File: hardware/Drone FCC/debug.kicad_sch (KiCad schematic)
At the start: 1 part, among them J22 Conn_02x05_Odd_Even

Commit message: finished IMU basic schematic
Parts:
- added J?: Conn_02x02_Counter_Clockwise, symbol Connector_Generic:Conn_02x02_Counter_Clockwise
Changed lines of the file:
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@@
     (pin "9")
   )
+  (symbol (lib_id "Connector_Generic:Conn_02x02_Counter_Clockwise") (at 104.775 75.565 0) (unit 1)
+    (in_bom yes) (on_board yes) (fields_autoplaced)
+    (property "Reference" "J?" (id 0) (at 106.045 68.58 0))
+    (property "Value" "Conn_02x02_Counter_Clockwise" (id 1) (at 106.045 71.12 0))
+    (property "Footprint" "" (id 2) (at 104.775 75.565 0)
+      (effects (font (size 1.27 1.27)) hide)
+    )
+    (property "Datasheet" "~" (id 3) (at 104.775 75.565 0)
+      (effects (font (size 1.27 1.27)) hide)
+    )
+    (pin "1")
+    (pin "2")
+    (pin "3")
+    (pin "4")
+  )
 )

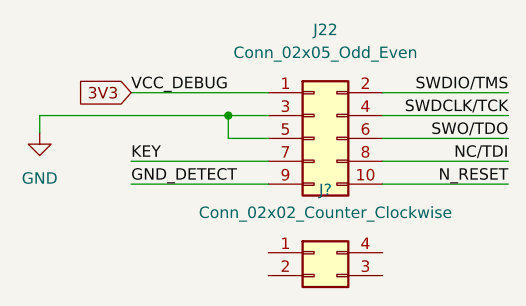
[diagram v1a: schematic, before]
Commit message: finish barometer schematic
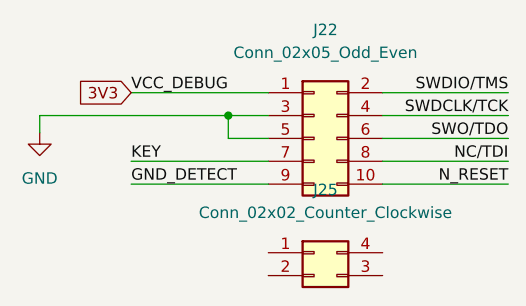
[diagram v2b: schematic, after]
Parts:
- gave numbers to parts that had none: 1
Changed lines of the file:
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@@
   (symbol (lib_id "Connector_Generic:Conn_02x02_Counter_Clockwise") (at 104.775 75.565 0) (unit 1)
     (in_bom yes) (on_board yes) (fields_autoplaced)
-    (property "Reference" "J?" (id 0) (at 106.045 68.58 0))
+    (property "Reference" "J25" (id 0) (at 106.045 68.58 0))
     (property "Value" "Conn_02x02_Counter_Clockwise" (id 1) (at 106.045 71.12 0))
     (property "Footprint" "" (id 2) (at 104.775 75.565 0)

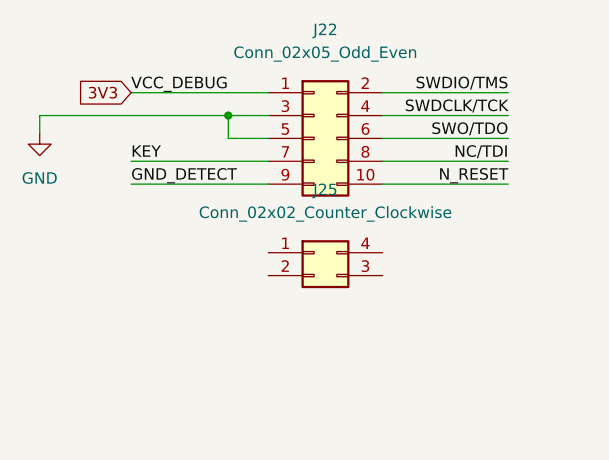
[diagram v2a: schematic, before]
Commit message: finish SWD functional schematic
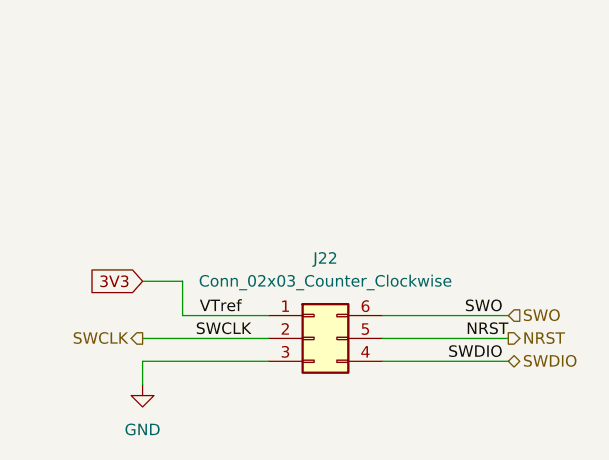
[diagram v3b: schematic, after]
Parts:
- removed J22: Conn_02x05_Odd_Even, FTSH-105-01-F-DV-K-TR:SAMTEC_FTSH-105-01-F-DV-P-TR, symbol Connector_Generic:Conn_02x05_Odd_Even
- removed J25: Conn_02x02_Counter_Clockwise, symbol Connector_Generic:Conn_02x02_Counter_Clockwise
- added J22: Conn_02x03_Counter_Clockwise, Connector_PinHeader_2.54mm:PinHeader_2x03_P2.54mm_Vertical, symbol Connector_Generic:Conn_02x03_Counter_Clockwise
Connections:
- net 3V3: now also J22.1 (Pin_1)
- net GND: now also J22.3 (Pin_3)
- new net NRST: J22.5 (Pin_5)
- new net SWCLK: J22.2 (Pin_2)
- new net SWDIO: J22.4 (Pin_4)
- new net SWO: J22.6 (Pin_6)
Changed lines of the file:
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@@
 (kicad_sch (version 20211123) (generator eeschema)
   (paper "A4")
-  (junction (at 95.25 60.325) (diameter 0) (color 0 0 0 0)
-  )
-  (wire (pts (xy 84.455 57.785) (xy 99.695 57.785))
+  (wire (pts (xy 90.17 78.74) (xy 90.17 82.55))
     (stroke (width 0) (type default) (color 0 0 0 0))
   )
-  (wire (pts (xy 95.25 62.865) (xy 95.25 60.325))
+  (wire (pts (xy 112.395 82.55) (xy 126.365 82.55))
     (stroke (width 0) (type default) (color 0 0 0 0))
   )
-  (wire (pts (xy 74.295 60.325) (xy 74.295 62.23))
+  (wire (pts (xy 85.725 87.63) (xy 99.695 87.63))
     (stroke (width 0) (type default) (color 0 0 0 0))
   )
-  (wire (pts (xy 112.395 62.865) (xy 126.365 62.865))
+  (wire (pts (xy 85.725 87.63) (xy 85.725 90.17))
     (stroke (width 0) (type default) (color 0 0 0 0))
   )
-  (wire (pts (xy 95.25 60.325) (xy 99.695 60.325))
+  (wire (pts (xy 112.395 85.09) (xy 126.365 85.09))
     (stroke (width 0) (type default) (color 0 0 0 0))
   )
-  (wire (pts (xy 84.455 67.945) (xy 99.695 67.945))
+  (wire (pts (xy 85.725 85.09) (xy 99.695 85.09))
     (stroke (width 0) (type default) (color 0 0 0 0))
   )
-  (wire (pts (xy 112.395 57.785) (xy 126.365 57.785))
+  (wire (pts (xy 112.395 87.63) (xy 126.365 87.63))
     (stroke (width 0) (type default) (color 0 0 0 0))
   )
-  (wire (pts (xy 84.455 65.405) (xy 99.695 65.405))
+  (wire (pts (xy 85.725 78.74) (xy 90.17 78.74))
     (stroke (width 0) (type default) (color 0 0 0 0))
   )
-  (wire (pts (xy 112.395 67.945) (xy 126.365 67.945))
+  (wire (pts (xy 90.17 82.55) (xy 99.695 82.55))
     (stroke (width 0) (type default) (color 0 0 0 0))
   )
-  (wire (pts (xy 99.695 62.865) (xy 95.25 62.865))
-    (stroke (width 0) (type default) (color 0 0 0 0))
+  (label "SWDIO" (at 125.73 87.63 180)
+    (effects (font (size 1.27 1.27)) (justify right bottom))
   )
-  (wire (pts (xy 74.295 60.325) (xy 95.25 60.325))
-    (stroke (width 0) (type default) (color 0 0 0 0))
-  )
-  (wire (pts (xy 112.395 60.325) (xy 126.365 60.325))
-    (stroke (width 0) (type default) (color 0 0 0 0))
-  )
-  (wire (pts (xy 112.395 65.405) (xy 126.365 65.405))
-    (stroke (width 0) (type default) (color 0 0 0 0))
-  )
-  (label "VCC_DEBUG" (at 84.455 57.785 0)
+  (label "VTref" (at 92.075 82.55 0)
     (effects (font (size 1.27 1.27)) (justify left bottom))
   )
-  (label "GND_DETECT" (at 84.455 67.945 0)
-    (effects (font (size 1.27 1.27)) (justify left bottom))
-  )
-  (label "N_RESET" (at 126.365 67.945 180)
+  (label "SWCLK" (at 97.79 85.09 180)
     (effects (font (size 1.27 1.27)) (justify right bottom))
   )
-  (label "SWO{slash}TDO" (at 126.365 62.865 180)
+  (label "NRST" (at 126.365 85.09 180)
     (effects (font (size 1.27 1.27)) (justify right bottom))
   )
-  (label "SWDCLK{slash}TCK" (at 126.365 60.325 180)
+  (label "SWO" (at 125.73 82.55 180)
     (effects (font (size 1.27 1.27)) (justify right bottom))
   )
-  (label "NC{slash}TDI" (at 126.365 65.405 180)
-    (effects (font (size 1.27 1.27)) (justify right bottom))
-  )
-  (label "SWDIO{slash}TMS" (at 126.365 57.785 180)
-    (effects (font (size 1.27 1.27)) (justify right bottom))
-  )
-  (label "KEY" (at 84.455 65.405 0)
-    (effects (font (size 1.27 1.27)) (justify left bottom))
-  )
-  (global_label "3V3" (shape input) (at 84.455 57.785 180) (fields_autoplaced)
+  (global_label "3V3" (shape input) (at 85.725 78.74 180) (fields_autoplaced)
     (effects (font (size 1.27 1.27)) (justify right))
-    (property "Intersheet References" "${INTERSHEET_REFS}" (id 0) (at 78.5343 57.7056 0)
+    (property "Intersheet References" "${INTERSHEET_REFS}" (id 0) (at 79.8043 78.6606 0)
       (effects (font (size 1.27 1.27)) (justify right) hide)
     )
   )
-  (symbol (lib_id "power:GND") (at 74.295 62.23 0) (unit 1)
+  (hierarchical_label "SWCLK" (shape output) (at 85.725 85.09 180)
+    (effects (font (size 1.27 1.27)) (justify right))
+  )
+  (hierarchical_label "NRST" (shape output) (at 126.365 85.09 0)
+    (effects (font (size 1.27 1.27)) (justify left))
+  )
+  (hierarchical_label "SWO" (shape input) (at 126.365 82.55 0)
+    (effects (font (size 1.27 1.27)) (justify left))
+  )
+  (hierarchical_label "SWDIO" (shape bidirectional) (at 126.365 87.63 0)
+    (effects (font (size 1.27 1.27)) (justify left))
+  )
+  (symbol (lib_id "power:GND") (at 85.725 90.17 0) (unit 1)
     (in_bom yes) (on_board yes) (fields_autoplaced)
-    (property "Reference" "#PWR0118" (id 0) (at 74.295 68.58 0)
+    (property "Reference" "#PWR0118" (id 0) (at 85.725 96.52 0)
       (effects (font (size 1.27 1.27)) hide)
     )
-    (property "Value" "GND" (id 1) (at 74.295 67.31 0))
-    (property "Footprint" "" (id 2) (at 74.295 62.23 0)
+    (property "Value" "GND" (id 1) (at 85.725 95.25 0))
+    (property "Footprint" "" (id 2) (at 85.725 90.17 0)
       (effects (font (size 1.27 1.27)) hide)
     )
-    (property "Datasheet" "" (id 3) (at 74.295 62.23 0)
+    (property "Datasheet" "" (id 3) (at 85.725 90.17 0)
       (effects (font (size 1.27 1.27)) hide)
     )
     (pin "1")
   )
-  (symbol (lib_id "Connector_Generic:Conn_02x05_Odd_Even") (at 104.775 62.865 0) (unit 1)
+  (symbol (lib_id "Connector_Generic:Conn_02x03_Counter_Clockwise") (at 104.775 85.09 0) (unit 1)
     (in_bom yes) (on_board yes) (fields_autoplaced)
-    (property "Reference" "J22" (id 0) (at 106.045 50.8 0))
-    (property "Value" "Conn_02x05_Odd_Even" (id 1) (at 106.045 53.34 0))
-    (property "Footprint" "FTSH-105-01-F-DV-K-TR:SAMTEC_FTSH-105-01-F-DV-P-TR" (id 2) (at 104.775 62.865 0)
+    (property "Reference" "J22" (id 0) (at 106.045 76.2 0))
+    (property "Value" "Conn_02x03_Counter_Clockwise" (id 1) (at 106.045 78.74 0))
+    (property "Footprint" "Connector_PinHeader_2.54mm:PinHeader_2x03_P2.54mm_Vertical" (id 2) (at 104.775 85.09 0)
       (effects (font (size 1.27 1.27)) hide)
     )
-    (property "Datasheet" "~" (id 3) (at 104.775 62.865 0)
-      (effects (font (size 1.27 1.27)) hide)
-    )
-    (pin "1")
-    (pin "10")
-    (pin "2")
-    (pin "3")
-    (pin "4")
-    (pin "5")
-    (pin "6")
-    (pin "7")
-    (pin "8")
-    (pin "9")
-  )
-  (symbol (lib_id "Connector_Generic:Conn_02x02_Counter_Clockwise") (at 104.775 75.565 0) (unit 1)
-    (in_bom yes) (on_board yes) (fields_autoplaced)
-    (property "Reference" "J25" (id 0) (at 106.045 68.58 0))
-    (property "Value" "Conn_02x02_Counter_Clockwise" (id 1) (at 106.045 71.12 0))
-    (property "Footprint" "" (id 2) (at 104.775 75.565 0)
-      (effects (font (size 1.27 1.27)) hide)
-    )
-    (property "Datasheet" "~" (id 3) (at 104.775 75.565 0)
+    (property "Datasheet" "~" (id 3) (at 104.775 85.09 0)
       (effects (font (size 1.27 1.27)) hide)
     )
@@
     (pin "3")
     (pin "4")
+    (pin "5")
+    (pin "6")
   )
 )

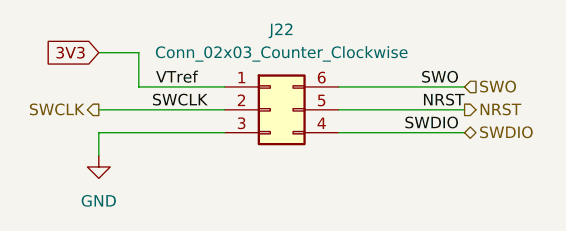
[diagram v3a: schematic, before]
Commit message: re enumeration of components
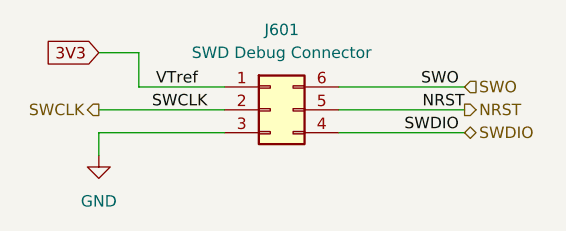
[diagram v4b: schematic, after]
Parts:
- J601: renamed from J22; value Conn_02x03_Counter_Clockwise -> SWD Debug Connector
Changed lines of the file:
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@@
   (symbol (lib_id "Connector_Generic:Conn_02x03_Counter_Clockwise") (at 104.775 85.09 0) (unit 1)
     (in_bom yes) (on_board yes) (fields_autoplaced)
-    (property "Reference" "J22" (id 0) (at 106.045 76.2 0))
-    (property "Value" "Conn_02x03_Counter_Clockwise" (id 1) (at 106.045 78.74 0))
+    (property "Reference" "J601" (id 0) (at 106.045 76.2 0))
+    (property "Value" "SWD Debug Connector" (id 1) (at 106.045 78.74 0))
     (property "Footprint" "Connector_PinHeader_2.54mm:PinHeader_2x03_P2.54mm_Vertical" (id 2) (at 104.775 85.09 0)
       (effects (font (size 1.27 1.27)) hide)

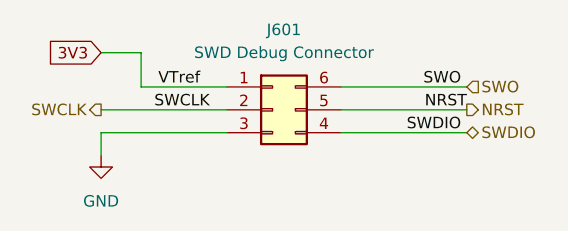
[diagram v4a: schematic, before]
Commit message: included all components on PCB
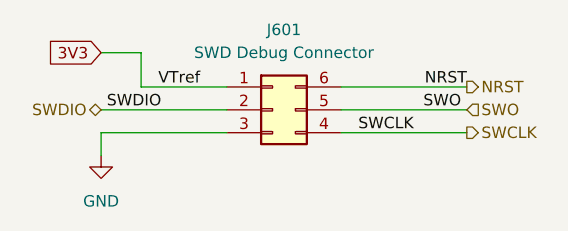
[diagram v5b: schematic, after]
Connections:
- net NRST: now also J601.6 (Pin_6); no longer J601.5 (Pin_5)
- net SWCLK: now also J601.4 (Pin_4); no longer J601.2 (Pin_2)
- net SWDIO: now also J601.2 (Pin_2); no longer J601.4 (Pin_4)
- net SWO: now also J601.5 (Pin_5); no longer J601.6 (Pin_6)
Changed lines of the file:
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@@
     (stroke (width 0) (type default) (color 0 0 0 0))
   )
-  (wire (pts (xy 112.395 82.55) (xy 126.365 82.55))
+  (wire (pts (xy 112.395 85.09) (xy 126.365 85.09))
     (stroke (width 0) (type default) (color 0 0 0 0))
   )
@@
     (stroke (width 0) (type default) (color 0 0 0 0))
   )
-  (wire (pts (xy 112.395 85.09) (xy 126.365 85.09))
+  (wire (pts (xy 112.395 82.55) (xy 126.365 82.55))
     (stroke (width 0) (type default) (color 0 0 0 0))
   )
-  (wire (pts (xy 85.725 85.09) (xy 99.695 85.09))
+  (wire (pts (xy 126.365 87.63) (xy 112.395 87.63))
     (stroke (width 0) (type default) (color 0 0 0 0))
   )
-  (wire (pts (xy 112.395 87.63) (xy 126.365 87.63))
+  (wire (pts (xy 99.695 85.09) (xy 85.725 85.09))
     (stroke (width 0) (type default) (color 0 0 0 0))
   )
@@
     (stroke (width 0) (type default) (color 0 0 0 0))
   )
-  (label "SWDIO" (at 125.73 87.63 180)
-    (effects (font (size 1.27 1.27)) (justify right bottom))
+  (label "SWDIO" (at 86.36 85.09 0)
+    (effects (font (size 1.27 1.27)) (justify left bottom))
   )
   (label "VTref" (at 92.075 82.55 0)
     (effects (font (size 1.27 1.27)) (justify left bottom))
   )
-  (label "SWCLK" (at 97.79 85.09 180)
+  (label "SWCLK" (at 114.3 87.63 0)
+    (effects (font (size 1.27 1.27)) (justify left bottom))
+  )
+  (label "NRST" (at 126.365 82.55 180)
     (effects (font (size 1.27 1.27)) (justify right bottom))
   )
-  (label "NRST" (at 126.365 85.09 180)
-    (effects (font (size 1.27 1.27)) (justify right bottom))
-  )
-  (label "SWO" (at 125.73 82.55 180)
+  (label "SWO" (at 125.73 85.09 180)
     (effects (font (size 1.27 1.27)) (justify right bottom))
   )
@@
     )
   )
-  (hierarchical_label "SWCLK" (shape output) (at 85.725 85.09 180)
+  (hierarchical_label "SWCLK" (shape output) (at 126.365 87.63 0)
+    (effects (font (size 1.27 1.27)) (justify left))
+  )
+  (hierarchical_label "NRST" (shape output) (at 126.365 82.55 0)
+    (effects (font (size 1.27 1.27)) (justify left))
+  )
+  (hierarchical_label "SWO" (shape input) (at 126.365 85.09 0)
+    (effects (font (size 1.27 1.27)) (justify left))
+  )
+  (hierarchical_label "SWDIO" (shape bidirectional) (at 85.725 85.09 180)
     (effects (font (size 1.27 1.27)) (justify right))
   )
-  (hierarchical_label "NRST" (shape output) (at 126.365 85.09 0)
-    (effects (font (size 1.27 1.27)) (justify left))
-  )
-  (hierarchical_label "SWO" (shape input) (at 126.365 82.55 0)
-    (effects (font (size 1.27 1.27)) (justify left))
-  )
-  (hierarchical_label "SWDIO" (shape bidirectional) (at 126.365 87.63 0)
-    (effects (font (size 1.27 1.27)) (justify left))
-  )
   (symbol (lib_id "power:GND") (at 85.725 90.17 0) (unit 1)

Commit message: finished
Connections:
- net 3V3: now also J601.2 (Pin_2); no longer J601.1 (Pin_1)
- net GND: now also J601.6 (Pin_6); no longer J601.3 (Pin_3)
- net NRST: now also J601.3 (Pin_3); no longer J601.6 (Pin_6)
- net SWDIO: now also J601.1 (Pin_1); no longer J601.2 (Pin_2)
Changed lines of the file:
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@@
 (kicad_sch (version 20211123) (generator eeschema)
   (paper "A4")
-  (wire (pts (xy 90.17 78.74) (xy 90.17 82.55))
-    (stroke (width 0) (type default) (color 0 0 0 0))
-  )
   (wire (pts (xy 112.395 85.09) (xy 126.365 85.09))
     (stroke (width 0) (type default) (color 0 0 0 0))
   )
-  (wire (pts (xy 85.725 87.63) (xy 99.695 87.63))
+  (wire (pts (xy 112.395 82.55) (xy 141.605 82.55))
     (stroke (width 0) (type default) (color 0 0 0 0))
   )
-  (wire (pts (xy 85.725 87.63) (xy 85.725 90.17))
+  (wire (pts (xy 141.605 82.55) (xy 141.605 85.09))
     (stroke (width 0) (type default) (color 0 0 0 0))
   )
-  (wire (pts (xy 112.395 82.55) (xy 126.365 82.55))
+  (wire (pts (xy 99.695 87.63) (xy 85.725 87.63))
     (stroke (width 0) (type default) (color 0 0 0 0))
   )
@@
     (stroke (width 0) (type default) (color 0 0 0 0))
   )
-  (wire (pts (xy 99.695 85.09) (xy 85.725 85.09))
+  (wire (pts (xy 99.695 82.55) (xy 85.725 82.55))
     (stroke (width 0) (type default) (color 0 0 0 0))
   )
-  (wire (pts (xy 85.725 78.74) (xy 90.17 78.74))
+  (wire (pts (xy 85.725 85.09) (xy 99.695 85.09))
     (stroke (width 0) (type default) (color 0 0 0 0))
   )
-  (wire (pts (xy 90.17 82.55) (xy 99.695 82.55))
-    (stroke (width 0) (type default) (color 0 0 0 0))
-  )
-  (label "SWDIO" (at 86.36 85.09 0)
+  (label "SWDIO" (at 86.36 82.55 0)
     (effects (font (size 1.27 1.27)) (justify left bottom))
   )
-  (label "VTref" (at 92.075 82.55 0)
+  (label "VTref" (at 92.075 85.09 0)
     (effects (font (size 1.27 1.27)) (justify left bottom))
   )
@@
     (effects (font (size 1.27 1.27)) (justify left bottom))
   )
-  (label "NRST" (at 126.365 82.55 180)
-    (effects (font (size 1.27 1.27)) (justify right bottom))
+  (label "NRST" (at 85.725 87.63 0)
+    (effects (font (size 1.27 1.27)) (justify left bottom))
   )
   (label "SWO" (at 125.73 85.09 180)
     (effects (font (size 1.27 1.27)) (justify right bottom))
   )
-  (global_label "3V3" (shape input) (at 85.725 78.74 180) (fields_autoplaced)
+  (global_label "3V3" (shape input) (at 85.725 85.09 180) (fields_autoplaced)
     (effects (font (size 1.27 1.27)) (justify right))
-    (property "Intersheet References" "${INTERSHEET_REFS}" (id 0) (at 79.8043 78.6606 0)
+    (property "Intersheet References" "${INTERSHEET_REFS}" (id 0) (at 79.8043 85.0106 0)
       (effects (font (size 1.27 1.27)) (justify right) hide)
     )
@@
     (effects (font (size 1.27 1.27)) (justify left))
   )
-  (hierarchical_label "NRST" (shape output) (at 126.365 82.55 0)
-    (effects (font (size 1.27 1.27)) (justify left))
+  (hierarchical_label "NRST" (shape output) (at 85.725 87.63 180)
+    (effects (font (size 1.27 1.27)) (justify right))
   )
   (hierarchical_label "SWO" (shape input) (at 126.365 85.09 0)
     (effects (font (size 1.27 1.27)) (justify left))
   )
-  (hierarchical_label "SWDIO" (shape bidirectional) (at 85.725 85.09 180)
+  (hierarchical_label "SWDIO" (shape bidirectional) (at 85.725 82.55 180)
     (effects (font (size 1.27 1.27)) (justify right))
   )
-  (symbol (lib_id "power:GND") (at 85.725 90.17 0) (unit 1)
+  (symbol (lib_id "power:GND") (at 141.605 85.09 0) (mirror y) (unit 1)
     (in_bom yes) (on_board yes) (fields_autoplaced)
-    (property "Reference" "#PWR0118" (id 0) (at 85.725 96.52 0)
+    (property "Reference" "#PWR0118" (id 0) (at 141.605 91.44 0)
       (effects (font (size 1.27 1.27)) hide)
     )
-    (property "Value" "GND" (id 1) (at 85.725 95.25 0))
-    (property "Footprint" "" (id 2) (at 85.725 90.17 0)
+    (property "Value" "GND" (id 1) (at 141.605 90.17 0))
+    (property "Footprint" "" (id 2) (at 141.605 85.09 0)
       (effects (font (size 1.27 1.27)) hide)
     )
-    (property "Datasheet" "" (id 3) (at 85.725 90.17 0)
+    (property "Datasheet" "" (id 3) (at 141.605 85.09 0)
       (effects (font (size 1.27 1.27)) hide)
     )

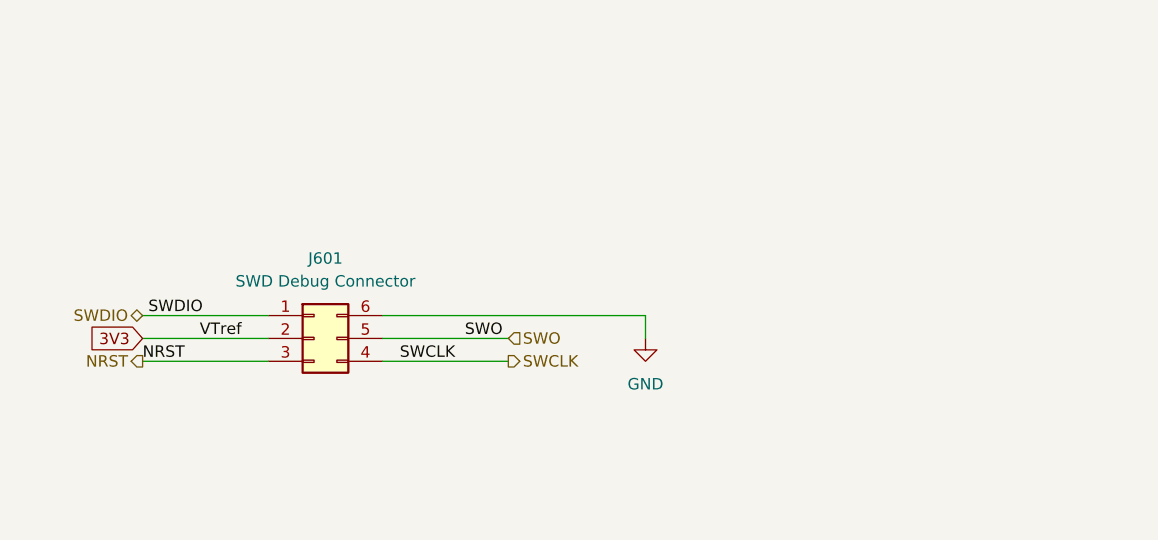
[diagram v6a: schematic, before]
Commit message: added missing TVS diodes
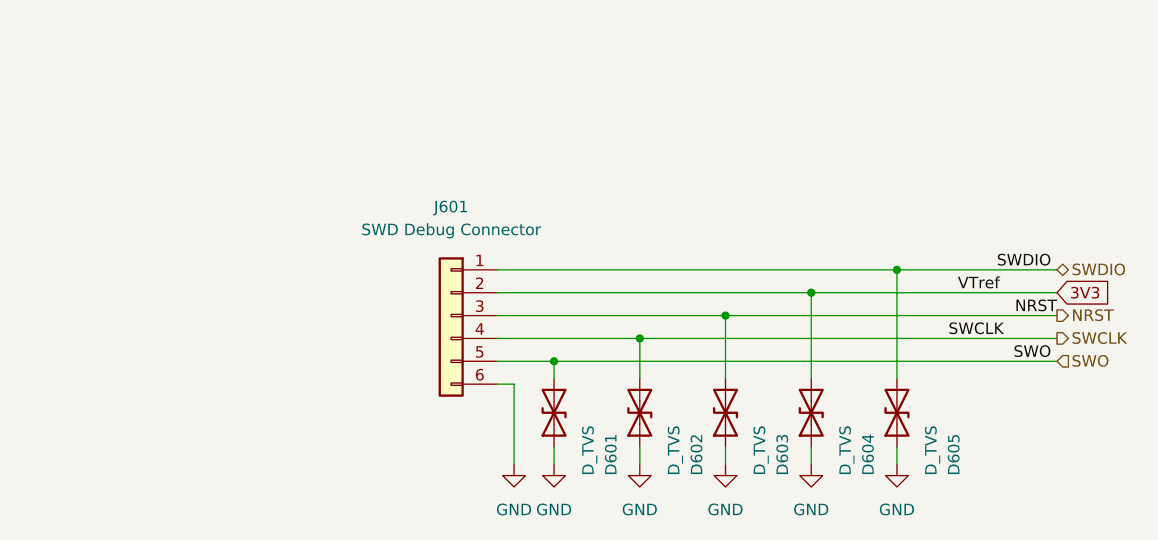
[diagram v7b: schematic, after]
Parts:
- removed J601: SWD Debug Connector, Connector_PinHeader_2.54mm:PinHeader_2x03_P2.54mm_Vertical, symbol Connector_Generic:Conn_02x03_Counter_Clockwise
- added D601, D602, D603, D604, D605: D_TVS, Diode_SMD:D_0402_1005Metric_Pad0.77x0.64mm_HandSolder, symbol Device:D_TVS
- added J601: SWD Debug Connector, Connector_PinHeader_2.54mm:PinHeader_2x03_P2.54mm_Vertical, symbol Connector_Generic:Conn_01x06
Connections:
- net 3V3: now also D604.2 (A2), J601.2 (Pin_2)
- net GND: now also D601.1 (A1), D602.1 (A1), D603.1 (A1), D604.1 (A1), D605.1 (A1), J601.6 (Pin_6)
- net NRST: now also D603.2 (A2), J601.3 (Pin_3)
- net SWCLK: now also D602.2 (A2), J601.4 (Pin_4)
- net SWDIO: now also D605.2 (A2), J601.1 (Pin_1)
- net SWO: now also D601.2 (A2), J601.5 (Pin_5)
